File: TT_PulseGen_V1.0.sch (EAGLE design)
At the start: 45 parts, among them IC1 4013N, IC2 4001N

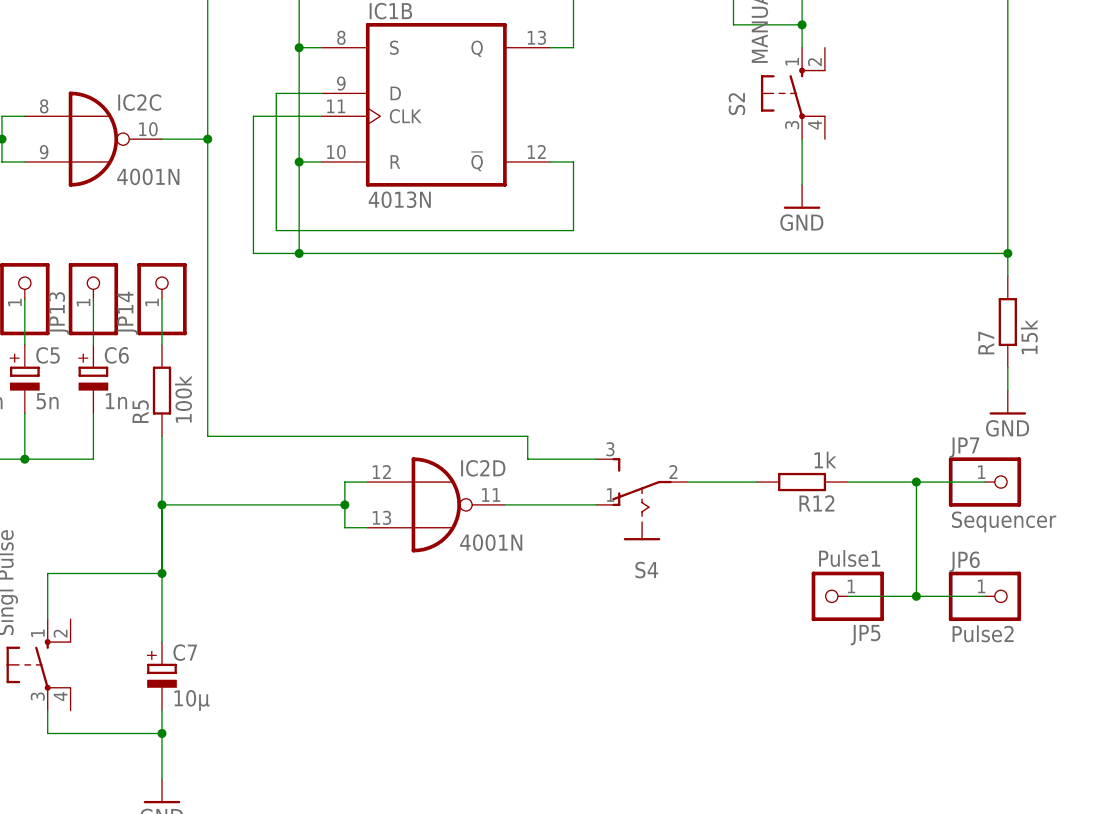
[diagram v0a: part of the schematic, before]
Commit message: Fixed pin 11 (and 10, 8, 4, 6, 7) on CD4013
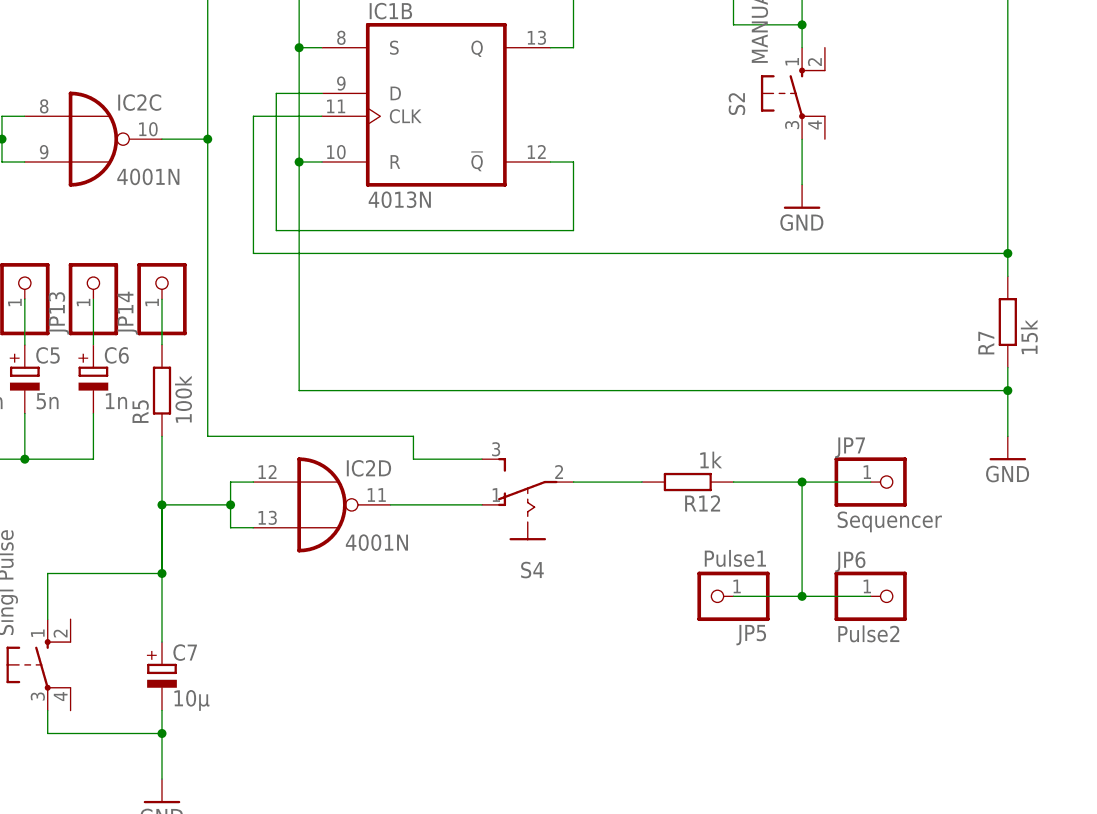
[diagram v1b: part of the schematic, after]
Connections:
- removed net N$13: IC1A.R, IC1A.S, IC1B.CLK, IC1B.R, IC1B.S, R7.2, T2.E
- new net N$33: IC1B.CLK, R7.2, T2.E
- net GND: now also IC1A.R, IC1A.S, IC1B.R, IC1B.S
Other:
- moved on the sheet: IC2D, JP5, JP6, JP7, R12, S4
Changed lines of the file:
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@@
 <instance part="IC2" gate="B" x="-22.86" y="38.1"/>
 <instance part="IC2" gate="C" x="20.32" y="38.1"/>
-<instance part="IC2" gate="D" x="58.42" y="-2.54"/>
+<instance part="IC2" gate="D" x="45.72" y="-2.54"/>
 <instance part="T1" gate="G$1" x="-76.2" y="10.16"/>
 <instance part="T2" gate="G$1" x="119.38" y="68.58"/>
@@
 <instance part="JP1" gate="G$1" x="-111.76" y="10.16" rot="R180"/>
 <instance part="R7" gate="G$1" x="121.92" y="17.78" rot="R90"/>
-<instance part="GND3" gate="1" x="121.92" y="7.62"/>
+<instance part="GND3" gate="1" x="121.92" y="2.54"/>
 <instance part="R8" gate="G$1" x="76.2" y="96.52" rot="R90"/>
 <instance part="R9" gate="G$1" x="86.36" y="96.52" rot="R90"/>
@@
 <instance part="JP2" gate="G$1" x="76.2" y="111.76" rot="R90"/>
 <instance part="JP3" gate="G$1" x="86.36" y="111.76" rot="R90"/>
-<instance part="R12" gate="G$1" x="99.06" y="0" rot="R180"/>
+<instance part="R12" gate="G$1" x="86.36" y="0" rot="R180"/>
 <instance part="JP4" gate="G$1" x="81.28" y="68.58" rot="R180"/>
-<instance part="S4" gate="1" x="81.28" y="-2.54" rot="R90"/>
-<instance part="JP5" gate="G$1" x="101.6" y="-12.7" rot="R180"/>
-<instance part="JP6" gate="G$1" x="121.92" y="-12.7"/>
-<instance part="JP7" gate="G$1" x="121.92" y="0"/>
+<instance part="S4" gate="1" x="68.58" y="-2.54" rot="R90"/>
+<instance part="JP5" gate="G$1" x="88.9" y="-12.7" rot="R180"/>
+<instance part="JP6" gate="G$1" x="109.22" y="-12.7"/>
+<instance part="JP7" gate="G$1" x="109.22" y="0"/>
 <instance part="JP8" gate="G$1" x="-17.78" y="22.86" rot="R90"/>
 <instance part="JP9" gate="G$1" x="-10.16" y="22.86" rot="R90"/>
@@
 <segment>
 <pinref part="IC2" gate="D" pin="I0"/>
-<wire x1="50.8" y1="0" x2="48.26" y2="0" width="0.1524" layer="91"/>
-<wire x1="48.26" y1="0" x2="48.26" y2="-2.54" width="0.1524" layer="91"/>
+<wire x1="38.1" y1="0" x2="35.56" y2="0" width="0.1524" layer="91"/>
+<wire x1="35.56" y1="0" x2="35.56" y2="-2.54" width="0.1524" layer="91"/>
 <pinref part="IC2" gate="D" pin="I1"/>
-<wire x1="48.26" y1="-2.54" x2="48.26" y2="-5.08" width="0.1524" layer="91"/>
-<wire x1="48.26" y1="-5.08" x2="50.8" y2="-5.08" width="0.1524" layer="91"/>
+<wire x1="35.56" y1="-2.54" x2="35.56" y2="-5.08" width="0.1524" layer="91"/>
+<wire x1="35.56" y1="-5.08" x2="38.1" y2="-5.08" width="0.1524" layer="91"/>
 <pinref part="R5" gate="G$1" pin="1"/>
 <pinref part="C7" gate="G$1" pin="+"/>
@@
 <wire x1="15.24" y1="-10.16" x2="27.94" y2="-10.16" width="0.1524" layer="91"/>
 <junction x="27.94" y="-10.16"/>
-<wire x1="48.26" y1="-2.54" x2="27.94" y2="-2.54" width="0.1524" layer="91"/>
+<wire x1="35.56" y1="-2.54" x2="27.94" y2="-2.54" width="0.1524" layer="91"/>
 <junction x="27.94" y="-2.54"/>
-<junction x="48.26" y="-2.54"/>
+<junction x="35.56" y="-2.54"/>
 </segment>
 </net>
@@
 <pinref part="GND3" gate="1" pin="GND"/>
 <wire x1="121.92" y1="12.7" x2="121.92" y2="10.16" width="0.1524" layer="91"/>
-</segment>
-</net>
-<net name="N$13" class="0">
-<segment>
-<pinref part="IC1" gate="B" pin="CLK"/>
-<wire x1="45.72" y1="40.64" x2="38.1" y2="40.64" width="0.1524" layer="91"/>
-<wire x1="38.1" y1="40.64" x2="38.1" y2="25.4" width="0.1524" layer="91"/>
-<wire x1="38.1" y1="25.4" x2="43.18" y2="25.4" width="0.1524" layer="91"/>
-<pinref part="T2" gate="G$1" pin="E"/>
-<wire x1="43.18" y1="25.4" x2="121.92" y2="25.4" width="0.1524" layer="91"/>
-<wire x1="121.92" y1="25.4" x2="121.92" y2="63.5" width="0.1524" layer="91"/>
-<pinref part="R7" gate="G$1" pin="2"/>
-<wire x1="121.92" y1="25.4" x2="121.92" y2="22.86" width="0.1524" layer="91"/>
 <pinref part="IC1" gate="B" pin="S"/>
+<wire x1="121.92" y1="10.16" x2="121.92" y2="5.08" width="0.1524" layer="91"/>
 <wire x1="45.72" y1="48.26" x2="43.18" y2="48.26" width="0.1524" layer="91"/>
 <wire x1="43.18" y1="48.26" x2="43.18" y2="35.56" width="0.1524" layer="91"/>
 <pinref part="IC1" gate="B" pin="R"/>
-<wire x1="43.18" y1="35.56" x2="43.18" y2="25.4" width="0.1524" layer="91"/>
+<wire x1="43.18" y1="35.56" x2="43.18" y2="10.16" width="0.1524" layer="91"/>
 <wire x1="45.72" y1="35.56" x2="43.18" y2="35.56" width="0.1524" layer="91"/>
 <junction x="43.18" y="35.56"/>
-<junction x="43.18" y="25.4"/>
 <pinref part="IC1" gate="A" pin="S"/>
 <wire x1="45.72" y1="78.74" x2="43.18" y2="78.74" width="0.1524" layer="91"/>
@@
 <junction x="43.18" y="48.26"/>
 <junction x="43.18" y="66.04"/>
-<junction x="121.92" y="25.4"/>
+<wire x1="43.18" y1="10.16" x2="121.92" y2="10.16" width="0.1524" layer="91"/>
+<junction x="121.92" y="10.16"/>
 </segment>
 </net>
@@
 <wire x1="33.02" y1="38.1" x2="27.94" y2="38.1" width="0.1524" layer="91"/>
 <wire x1="33.02" y1="38.1" x2="33.02" y2="5.08" width="0.1524" layer="91"/>
-<wire x1="33.02" y1="5.08" x2="68.58" y2="5.08" width="0.1524" layer="91"/>
-<wire x1="68.58" y1="5.08" x2="68.58" y2="2.54" width="0.1524" layer="91"/>
+<wire x1="33.02" y1="5.08" x2="55.88" y2="5.08" width="0.1524" layer="91"/>
+<wire x1="55.88" y1="5.08" x2="55.88" y2="2.54" width="0.1524" layer="91"/>
 <pinref part="S4" gate="1" pin="S"/>
-<wire x1="68.58" y1="2.54" x2="76.2" y2="2.54" width="0.1524" layer="91"/>
+<wire x1="55.88" y1="2.54" x2="63.5" y2="2.54" width="0.1524" layer="91"/>
 <junction x="33.02" y="38.1"/>
 </segment>
@@
 <pinref part="S4" gate="1" pin="O"/>
 <pinref part="IC2" gate="D" pin="O"/>
-<wire x1="76.2" y1="-2.54" x2="66.04" y2="-2.54" width="0.1524" layer="91"/>
+<wire x1="63.5" y1="-2.54" x2="53.34" y2="-2.54" width="0.1524" layer="91"/>
 </segment>
 </net>
@@
 <segment>
 <pinref part="S4" gate="1" pin="P"/>
-<wire x1="86.36" y1="0" x2="93.98" y2="0" width="0.1524" layer="91"/>
+<wire x1="73.66" y1="0" x2="81.28" y2="0" width="0.1524" layer="91"/>
 <pinref part="R12" gate="G$1" pin="2"/>
 </segment>
@@
 <segment>
 <pinref part="R12" gate="G$1" pin="1"/>
-<wire x1="104.14" y1="0" x2="111.76" y2="0" width="0.1524" layer="91"/>
-<wire x1="111.76" y1="0" x2="119.38" y2="0" width="0.1524" layer="91"/>
-<wire x1="111.76" y1="0" x2="111.76" y2="-12.7" width="0.1524" layer="91"/>
-<wire x1="111.76" y1="-12.7" x2="104.14" y2="-12.7" width="0.1524" layer="91"/>
-<wire x1="111.76" y1="-12.7" x2="119.38" y2="-12.7" width="0.1524" layer="91"/>
+<wire x1="91.44" y1="0" x2="99.06" y2="0" width="0.1524" layer="91"/>
+<wire x1="99.06" y1="0" x2="106.68" y2="0" width="0.1524" layer="91"/>
+<wire x1="99.06" y1="0" x2="99.06" y2="-12.7" width="0.1524" layer="91"/>
+<wire x1="99.06" y1="-12.7" x2="91.44" y2="-12.7" width="0.1524" layer="91"/>
+<wire x1="99.06" y1="-12.7" x2="106.68" y2="-12.7" width="0.1524" layer="91"/>
 <pinref part="JP5" gate="G$1" pin="1"/>
 <pinref part="JP6" gate="G$1" pin="1"/>
 <pinref part="JP7" gate="G$1" pin="1"/>
-<junction x="111.76" y="-12.7"/>
-<junction x="111.76" y="0"/>
+<junction x="99.06" y="-12.7"/>
+<junction x="99.06" y="0"/>
 </segment>
 </net>
@@
 </segment>
 </net>
+<net name="N$33" class="0">
+<segment>
+<pinref part="IC1" gate="B" pin="CLK"/>
+<wire x1="45.72" y1="40.64" x2="38.1" y2="40.64" width="0.1524" layer="91"/>
+<wire x1="38.1" y1="40.64" x2="38.1" y2="25.4" width="0.1524" layer="91"/>
+<pinref part="T2" gate="G$1" pin="E"/>
+<wire x1="121.92" y1="22.86" x2="121.92" y2="25.4" width="0.1524" layer="91"/>
+<pinref part="R7" gate="G$1" pin="2"/>
+<wire x1="121.92" y1="25.4" x2="121.92" y2="63.5" width="0.1524" layer="91"/>
+<wire x1="38.1" y1="25.4" x2="121.92" y2="25.4" width="0.1524" layer="91"/>
+<junction x="121.92" y="25.4"/>
+</segment>
+</net>
